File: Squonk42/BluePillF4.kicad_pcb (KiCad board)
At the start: 2 copper layers, 53.3 x 22.9 mm, 159 parts, among them J1 MH20-1, J2 MH20-1, J3 MH_RA4-1, J4 MR07C-06200, J5 47642-001, U1 AP2114HA-3.3TRG1, U2 AP2112K3.3-TRG1, U3 STM32F405RGT6, U4 SY6280, Y1 FC-12M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

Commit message: Removed R12 pull-up resistoron SDIO_D3 Added R12 resistor to connect VBUS and PA9 for VBUS_SENSE (USB Host) feature Added C18 parallel decoupling capacitor on SDCard connector Added C19 parallel decoupling capacitor on LDO U1 output
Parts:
- added C18: 100n, BluePillF4 Lib:C0603, F.Cu at (88.8, 66.1)
- added C19: 100n, BluePillF4 Lib:C0603, F.Cu at (91.0, 66.1)
- J5: value 47642-001 -> U02-BFD3111B0-009
- R12: value 100k -> 510R
- moved R12 10.7 mm to (90.6, 55.3), turned to 0 degrees
- moved C16 2.95 mm to (92.6, 65.9), turned to 270 degrees
- moved R7 1.77 mm to (92.5, 56.0), turned to 270 degrees
- moved REF** 1.47 mm to (90.0, 65.6)
- moved C11 1.02 mm to (94.4, 56.6)
- moved C8 0.70 mm to (87.5, 66.1), turned to 90 degrees
- moved R13 0.25 mm to (88.0, 55.3)
- moved U4 0.25 mm to (84.9, 56.2)
- moved D3 0.25 mm to (89.3, 57.1)
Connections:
- R12 pad 1: /SDIO_D3 -> /VBUS
- R12 pad 2: +3V3 -> /PA9
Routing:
- net /PA9: track 15.7 -> 27.0 mm, vias 1 -> 3
- net /SDIO_D3: track 22.2 -> 18.8 mm, vias 2 -> 1
- net /VBUS: track 8.98 -> 11.8 mm
- net /VCAP_1: track 6.57 -> 5.46 mm

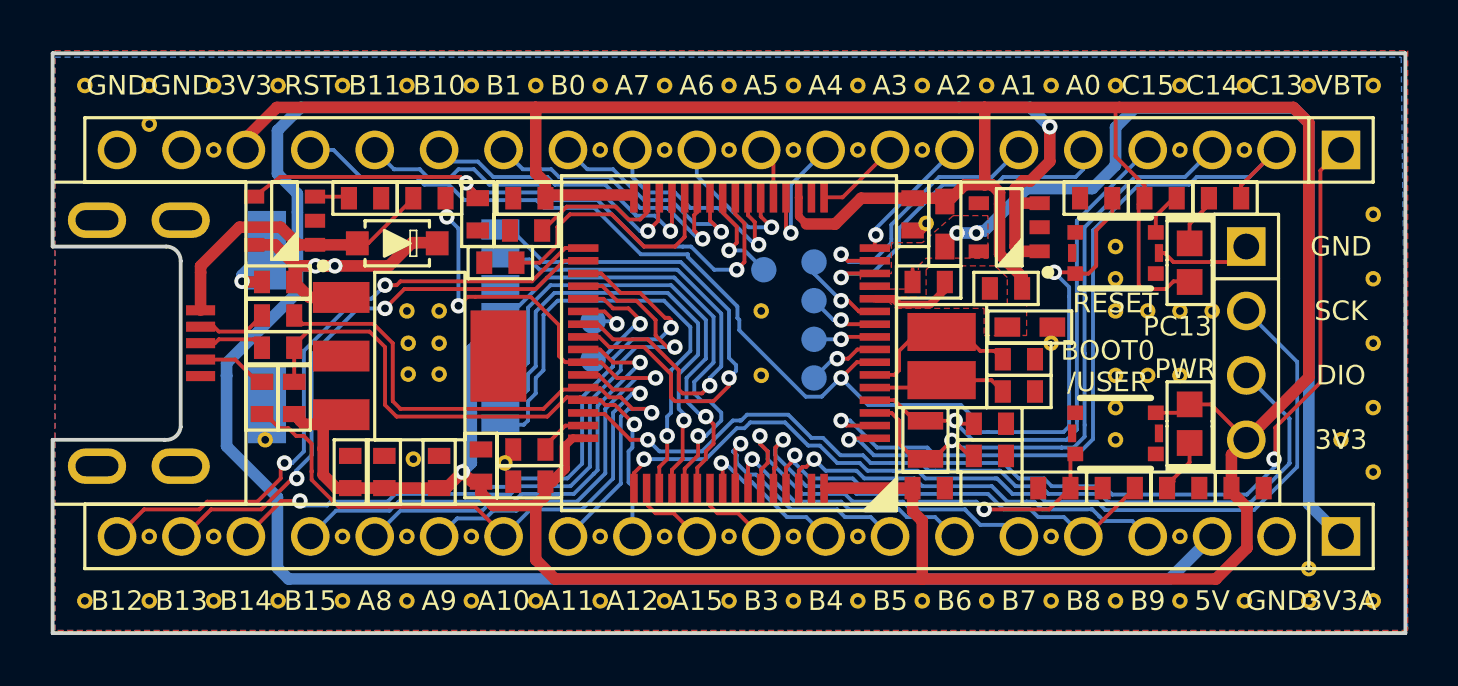
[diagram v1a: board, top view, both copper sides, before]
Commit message: Added RGB LED Added pull-down resistor on SDIO_D3 for SDCard detect feature
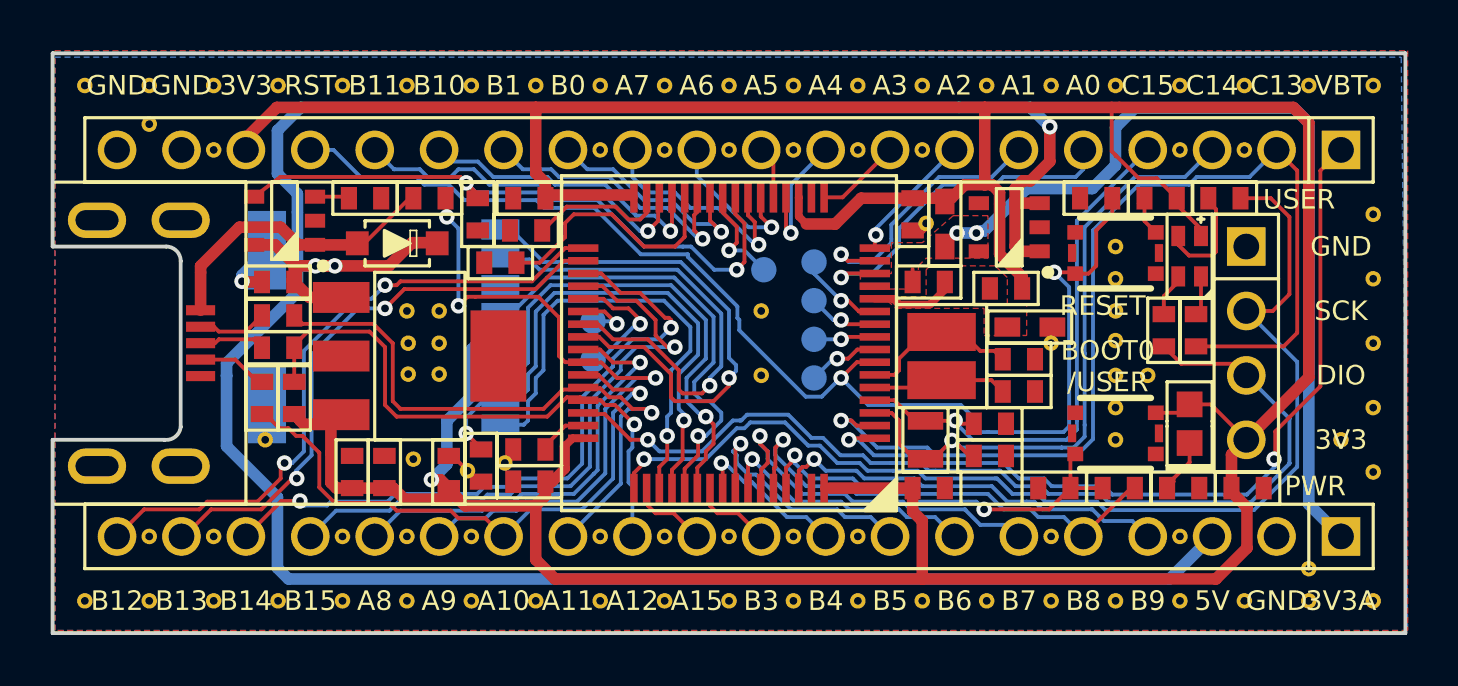
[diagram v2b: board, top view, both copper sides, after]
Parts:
- removed C19: 100n, BluePillF4 Lib:C0603
- added R14: 560R, BluePillF4 Lib:R0603, F.Cu at (119.5, 60.6)
- added R15: 220R, BluePillF4 Lib:R0603, F.Cu at (121.9, 55.3)
- added R16: 1M, BluePillF4 Lib:R0603, F.Cu at (92.6, 65.9)
- added REF**: VIA_12MIL, BluePillF4 Lib:VIA_12MIL, F.Cu at (92.1, 66.1)
- D2: value RED -> 1616RGB; footprint BluePillF4 Lib:LED0603 -> BluePillF4 Lib:1616RGB
- R3: value 510R -> 560R
- moved R3 5.33 mm to (120.8, 60.6), turned to 90 degrees
- moved REF** 1.73 mm to (117.6, 61.0)
- moved C16 1.30 mm to (91.4, 66.1)
- moved D2 0.25 mm to (120.6, 57.6), turned to 90 degrees
- moved C8 0.08 mm to (87.5, 66.1)
- turned R6 to 180 degrees
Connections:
- net /D2 renamed /D2_R
- D2 pad 2: +3V3 -> /D2_G
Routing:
- net /PC13: track 31.5 -> 40.7 mm
- net /PA14: track 36.8 -> 44.1 mm
- net /D2_B: track 0.00 -> 4.31 mm
- net /PA13: track 35.5 -> 39.2 mm
- net /SDIO_D3: track 18.8 -> 22.0 mm, vias 1 -> 2
- net GND: track 8.49 -> 6.49 mm
- net /D2_G: track 0.00 -> 1.72 mm
- net +3V3: track 162.3 -> 161.4 mm
- net /D2_R: track 2.09 -> 1.57 mm
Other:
- board text added: "USER"
- board text removed: "PC13"

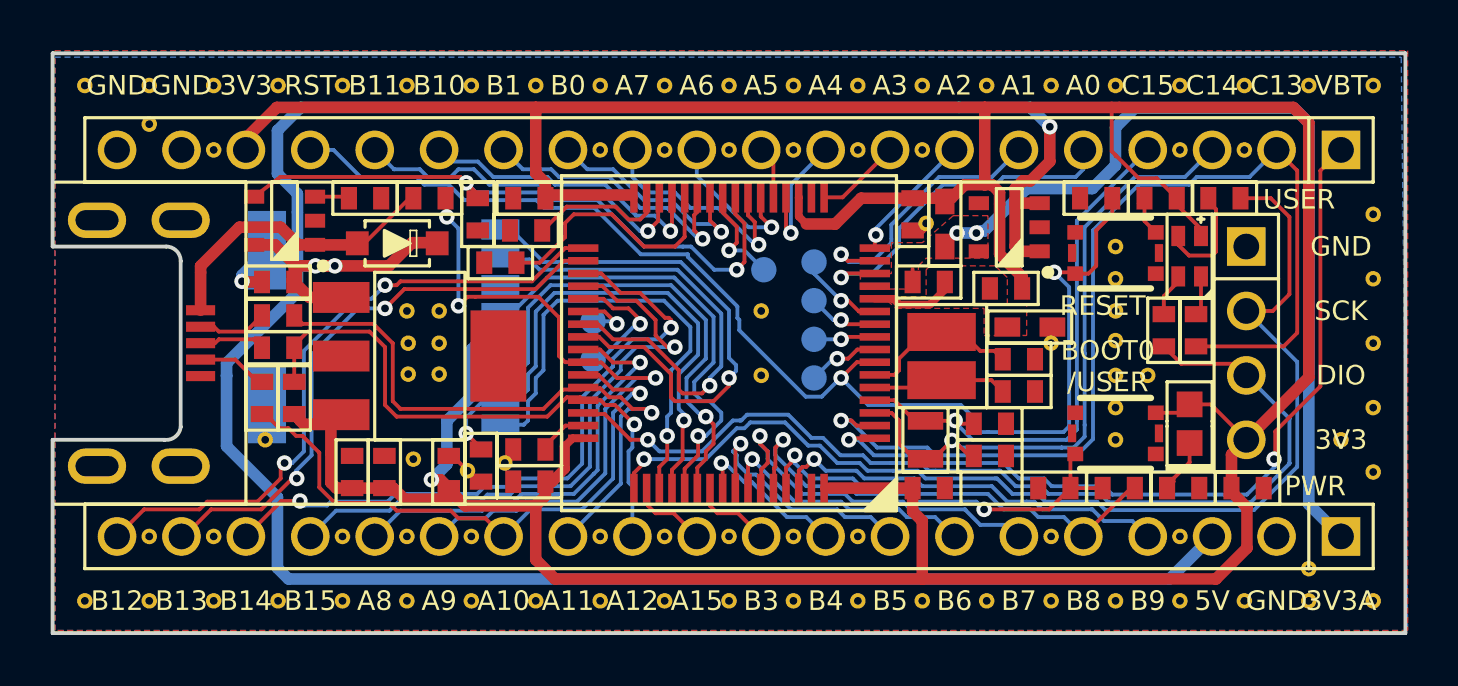
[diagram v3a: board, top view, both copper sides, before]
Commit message: Added inductor on SDIO_VDD to prevent transcient upon hot SDCard insertion
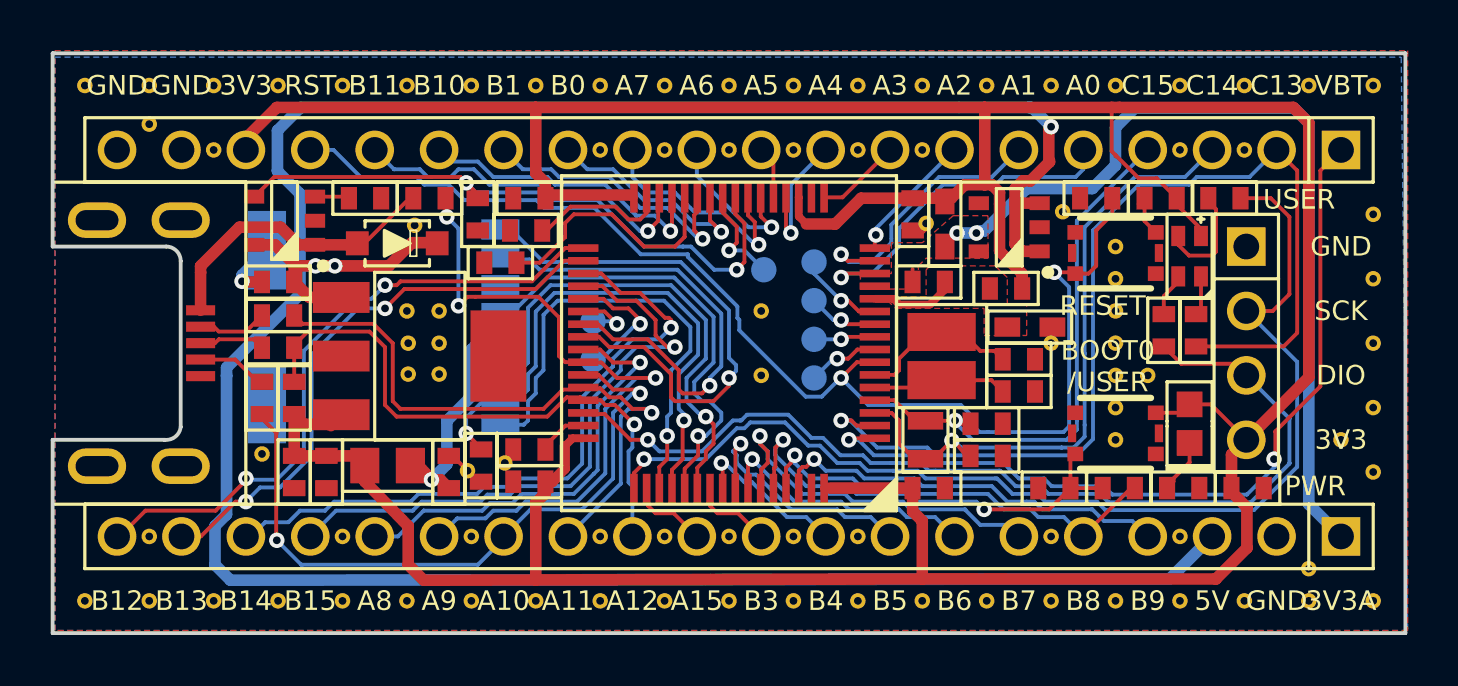
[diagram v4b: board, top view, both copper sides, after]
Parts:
- added L3: LQW2BASR47J00L, BluePillF4 Lib:FB0805, F.Cu at (88.9, 65.9)
- added REF**: VIA_12MIL, BluePillF4 Lib:VIA_12MIL, F.Cu at (115.6, 55.9)
- added REF**: VIA_12MIL, BluePillF4 Lib:VIA_12MIL, F.Cu at (90.0, 56.4)
- moved C18 2.29 mm to (86.5, 66.1), turned to 90 degrees
- moved C8 2.29 mm to (85.3, 66.1), turned to 270 degrees
- moved REF** 1.51 mm to (89.1, 64.4)
- moved REF** 0.57 mm to (84.0, 65.4)
- moved C2 0.13 mm to (112.6, 65.5)
- moved C3 0.13 mm to (112.6, 64.2)
- moved REF** 0.10 mm to (117.6, 61.1)
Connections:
- C16 pad 2: +3V3 -> /SDIO_VDD
- J4 pad P4: +3V3 -> /SDIO_VDD
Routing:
- net /SDIO_VDD: track 0.00 -> 9.01 mm, vias 0 -> 1
- net +3V3: track 161.4 -> 157.2 mm, vias 1 -> 0
- net /PA10: track 24.2 -> 26.9 mm, vias 1 -> 2
- net +5V: track 110.4 -> 112.4 mm
- net /PB12: track 25.7 -> 26.3 mm
- net /PB14: track 26.6 -> 26.4 mm, vias 2 -> 1

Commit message: Cleanup Tracks and Vias
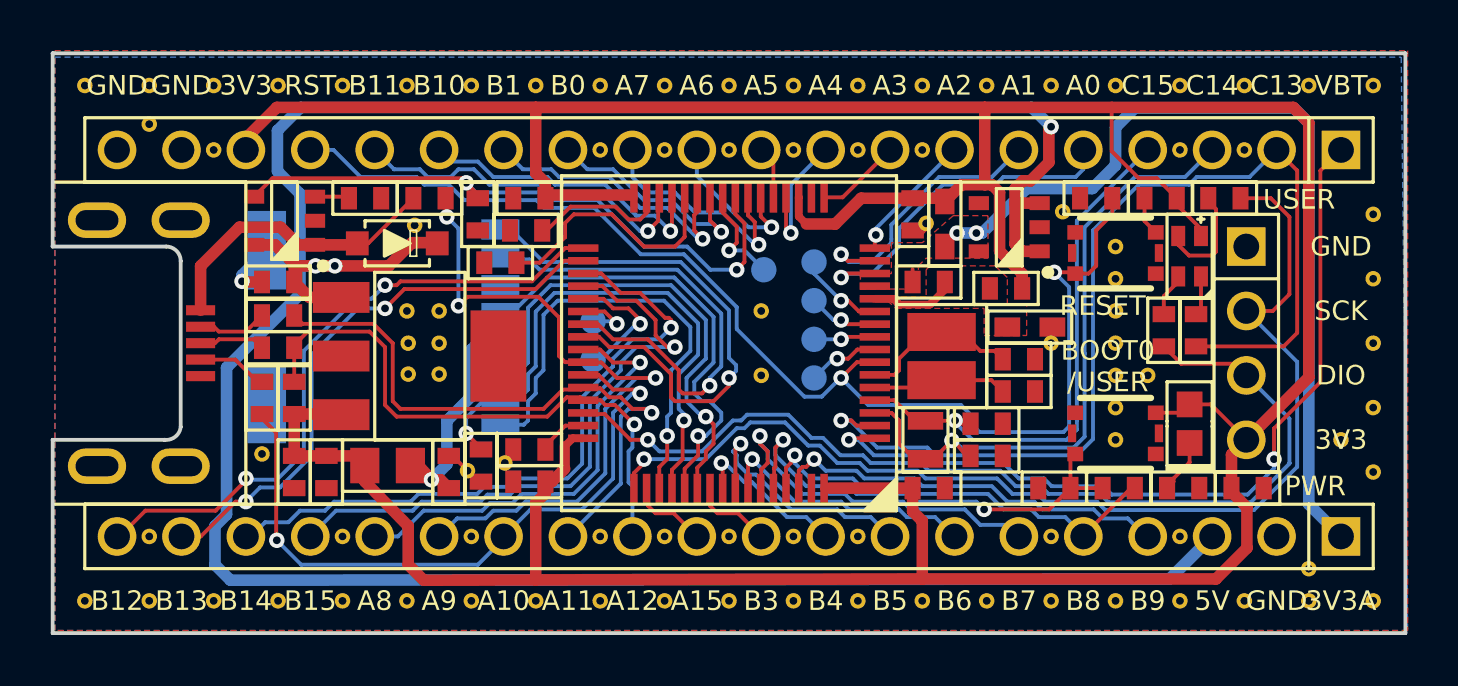
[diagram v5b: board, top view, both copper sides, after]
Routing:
- net +5V: track 112.4 -> 110.7 mm
- net +3V3: track 157.2 -> 155.8 mm
- net /PB12: track 26.3 -> 25.5 mm
